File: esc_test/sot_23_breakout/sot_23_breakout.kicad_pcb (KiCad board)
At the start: 2 copper layers, 10.7 x 5.3 mm, 3 parts, among them P1 CONN_01X02, P2 CONN_01X02, Q1 Q_NMOS_GDS

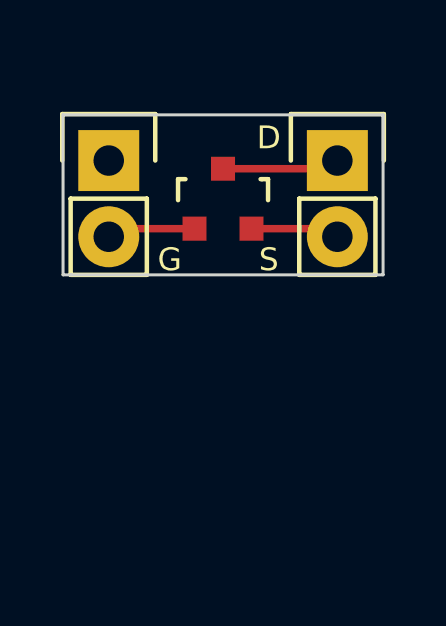
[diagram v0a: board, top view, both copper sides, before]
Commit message: Final test breakout boards sent to Oshpark.
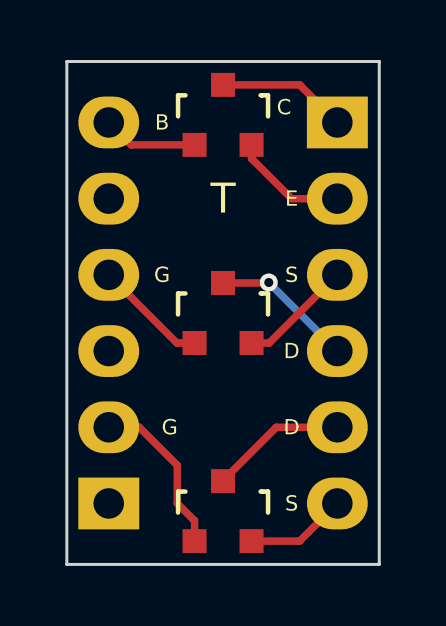
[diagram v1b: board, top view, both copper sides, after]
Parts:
- added Q2: P, Housings_SOT-23_SOT-143_TSOT-6:SOT-23, F.Cu at (141.7, 109.2)
- added Q3: N, Housings_SOT-23_SOT-143_TSOT-6:SOT-23, F.Cu at (141.7, 115.8)
- P1, P2: value CONN_01X02 -> CONN_01X06; footprint Pin_Headers:Pin_Header_Straight_1x02 -> esc:Pin_Header_Straight_1x06_no_outline
- Q1: value Q_NMOS_GDS -> Q_NPN_BEC
- moved P1 11.4 mm to (137.9, 115.6), turned to 180 degrees
- moved Q1 2.79 mm to (141.7, 102.6)
- moved P2 1.27 mm to (145.5, 102.9)
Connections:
- P1 pad 1: Net-(P1-Pad1) -> (no net)
- Q1 pad 1: Net-(P1-Pad2) -> Net-(P1-Pad6)
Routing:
- net Net-(P2-Pad4): track 0.00 -> 4.76 mm, vias 0 -> 1
- net Net-(P2-Pad5): track 0.00 -> 4.56 mm
- net Net-(P2-Pad3): track 0.00 -> 3.80 mm
- net Net-(P1-Pad4): track 0.00 -> 3.80 mm
- net Net-(P2-Pad6): track 0.00 -> 3.38 mm
- net Net-(P1-Pad6): track 0.00 -> 3.17 mm
- net Net-(P1-Pad2): track 2.97 -> 5.57 mm
- net Net-(P2-Pad2): track 2.97 -> 3.87 mm
- removed copper zone on B.Cu, net (none)
- removed copper zone on F.Cu, net (none)
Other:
- board size 10.7 x 5.3 mm -> 10.4 x 16.8 mm
- board text added: "B"
- board text added: "C"
- board text added: "E"
- board text added: "T"
